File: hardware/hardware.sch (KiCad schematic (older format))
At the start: 6 parts

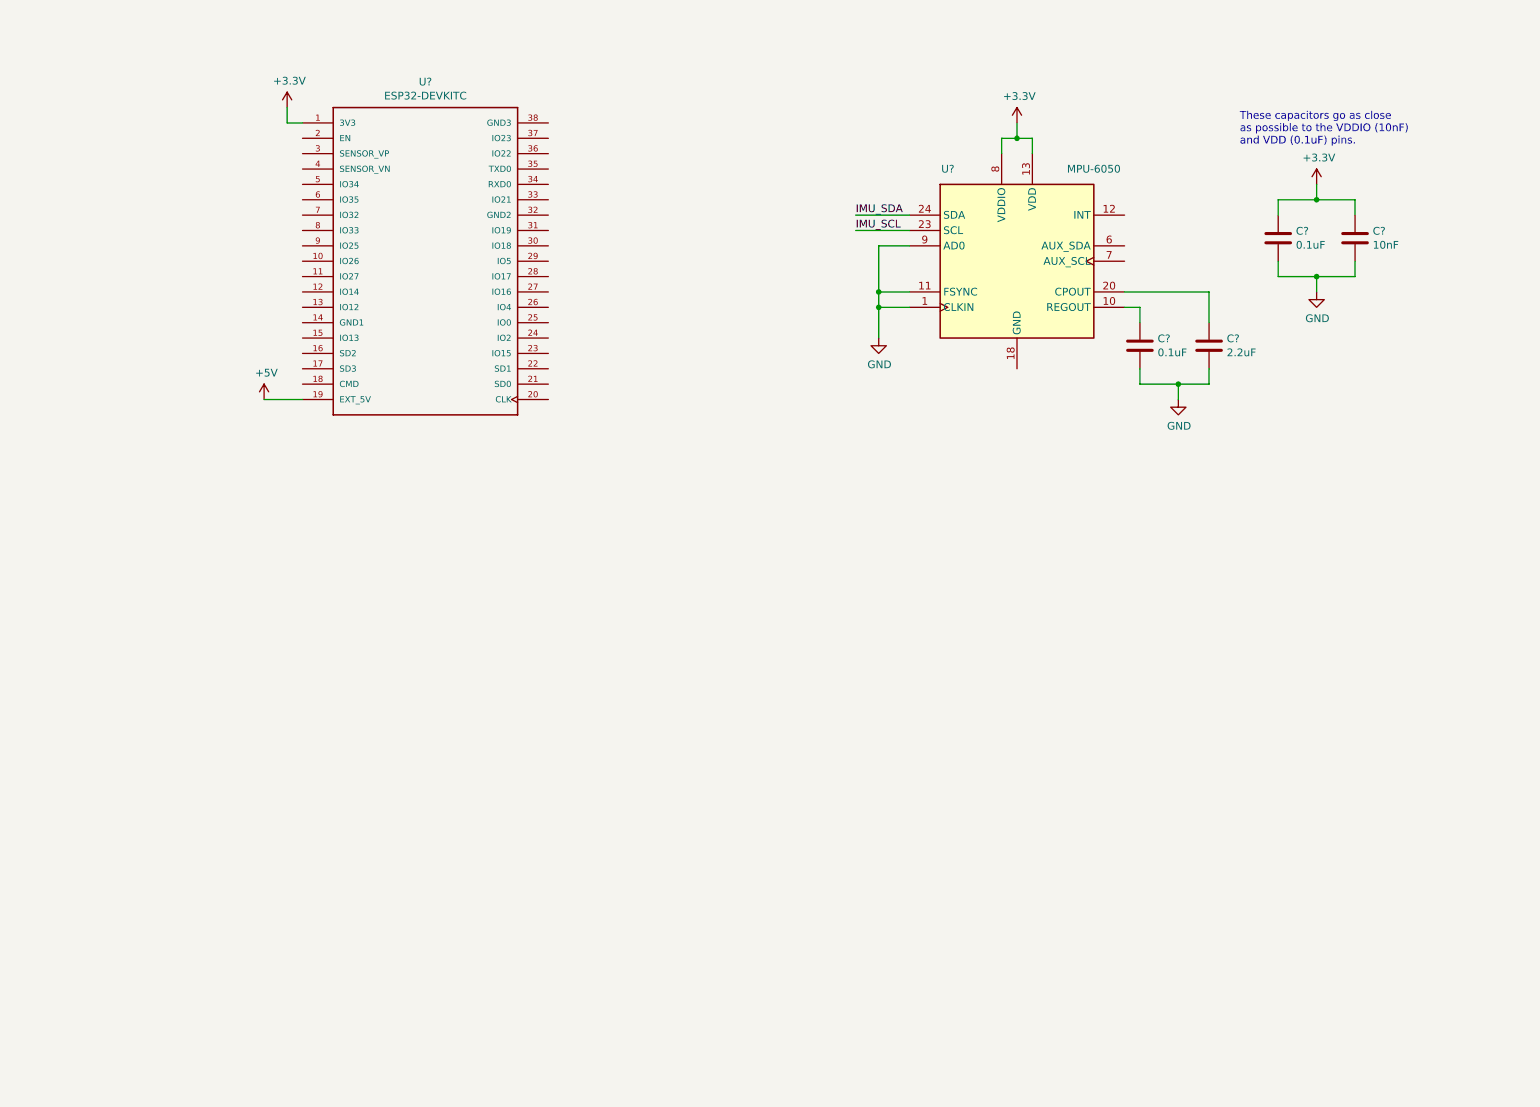
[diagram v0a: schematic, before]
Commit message: add cap sensor to schematic
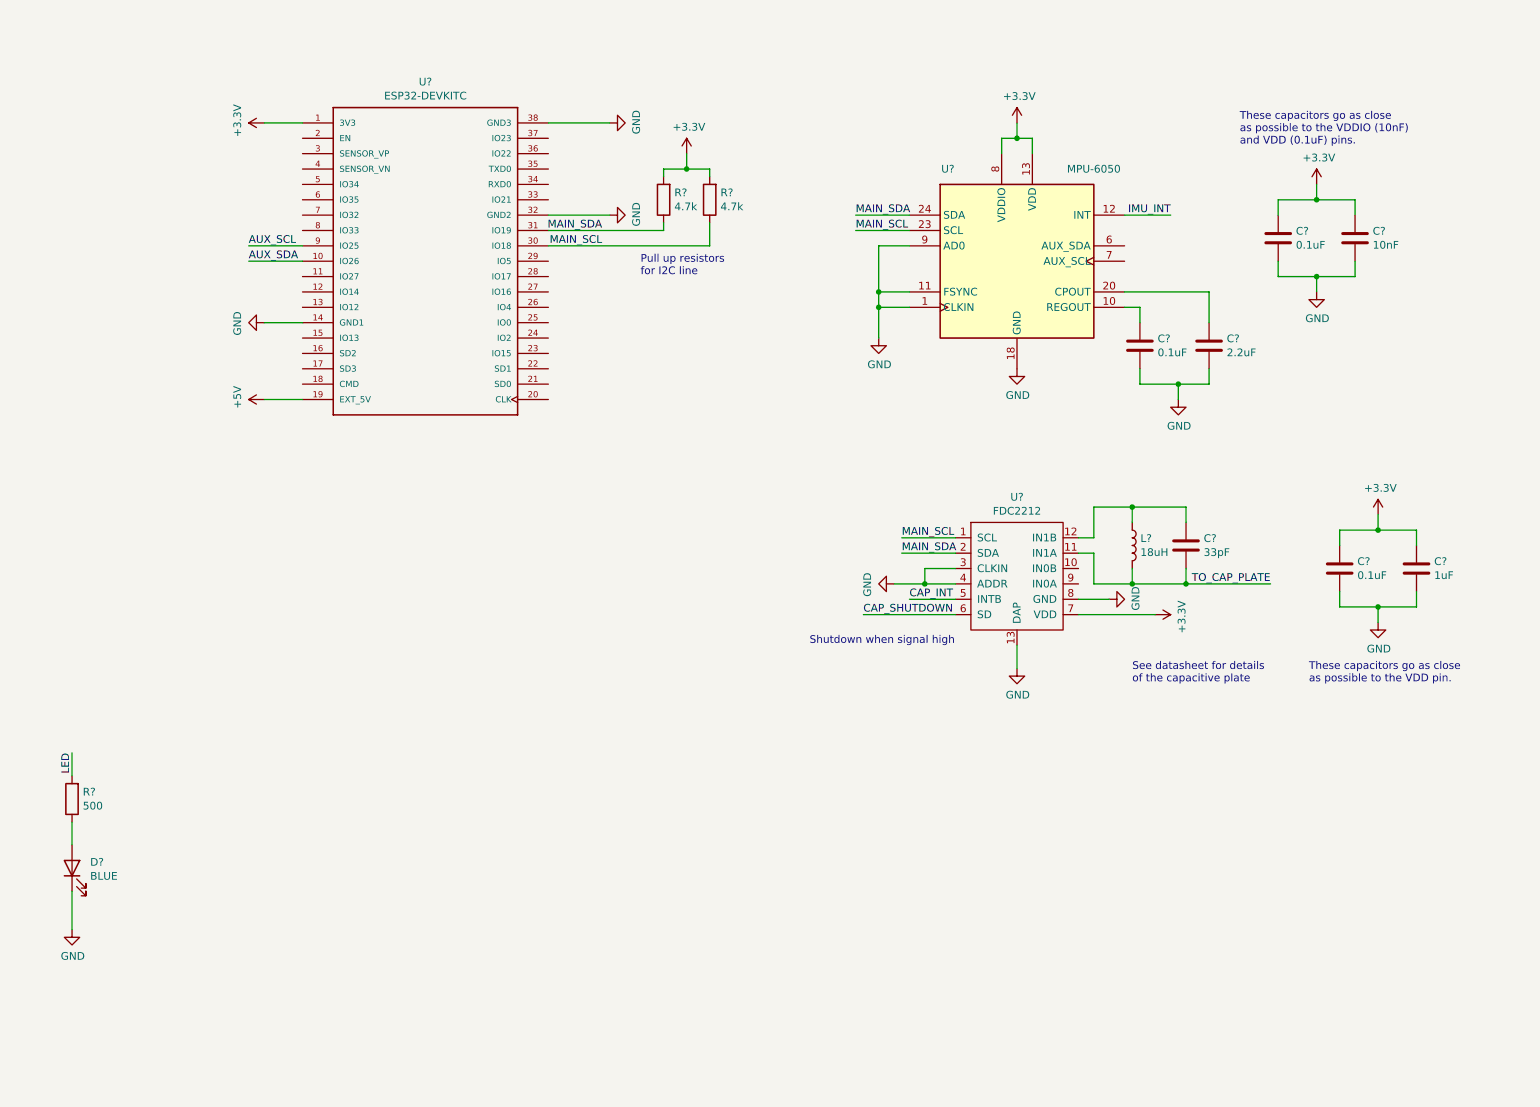
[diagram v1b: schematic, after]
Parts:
- added C?: 0.1uF, symbol Device:C
- added C?: 1uF, symbol Device:C
- added C?: 33pF, symbol Device:C
- added D?: BLUE, symbol Device:LED
- added L?: 18uH, symbol Device:L
- added R?: 500, symbol Device:R
- added R? (x2): 4.7k, symbol Device:R
- added U?: FDC2212, Package_SON:WSON-12-1EP_4x4mm_P0.5mm_EP2.6x3mm, symbol TI_FDC:FDC2212
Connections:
- net IMU_SCL is gone; now on net MAIN_SCL: U?.23 (SCL)
- net IMU_SDA is gone; now on net MAIN_SDA: U?.24 (SDA)
- net +3V3: now also C?.2, C?.2, R?.2, R?.2, U?.7 (VDD)
- net GND: now also U?.14 (GND1), U?.18 (GND), U?.32 (GND2), U?.38 (GND3), C?.1, C?.1, D?.1 (K), U?.13 (DAP), U?.3 (CLKIN), U?.4 (ADDR), U?.8 (GND)
- net AUX_SDA: now reaches U?.10 (IO26)
- net MAIN_SCL: now reaches U?.30 (IO18)
- net MAIN_SCL: now also R?.1, U?.1 (SCL)
- net MAIN_SDA: now reaches U?.31 (IO19)
- net MAIN_SDA: now also R?.1, U?.2 (SDA)
- net AUX_SCL: now reaches U?.9 (IO25)
- net IMU_INT: now reaches U?.12 (INT)
- new net: D?.2 (A), R?.1
- new net: C?.1, L?.1, U?.12 (IN1B)
- new net CAP_INT: U?.5 (INTB)
- new net CAP_SHUTDOWN: U?.6 (SD)
- new net LED: R?.2
- new net TO_CAP_PLATE: C?.2, L?.2, U?.11 (IN1A)
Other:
- note added: "Pull up resistors\nfor I2C line"
- note added: "See datasheet for details\nof the capacitive plate"
- note added: "Shutdown when signal high"
- note added: "These capacitors go as close\nas possible to the VDD pin."

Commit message: add acoustic and force sensor in schematic
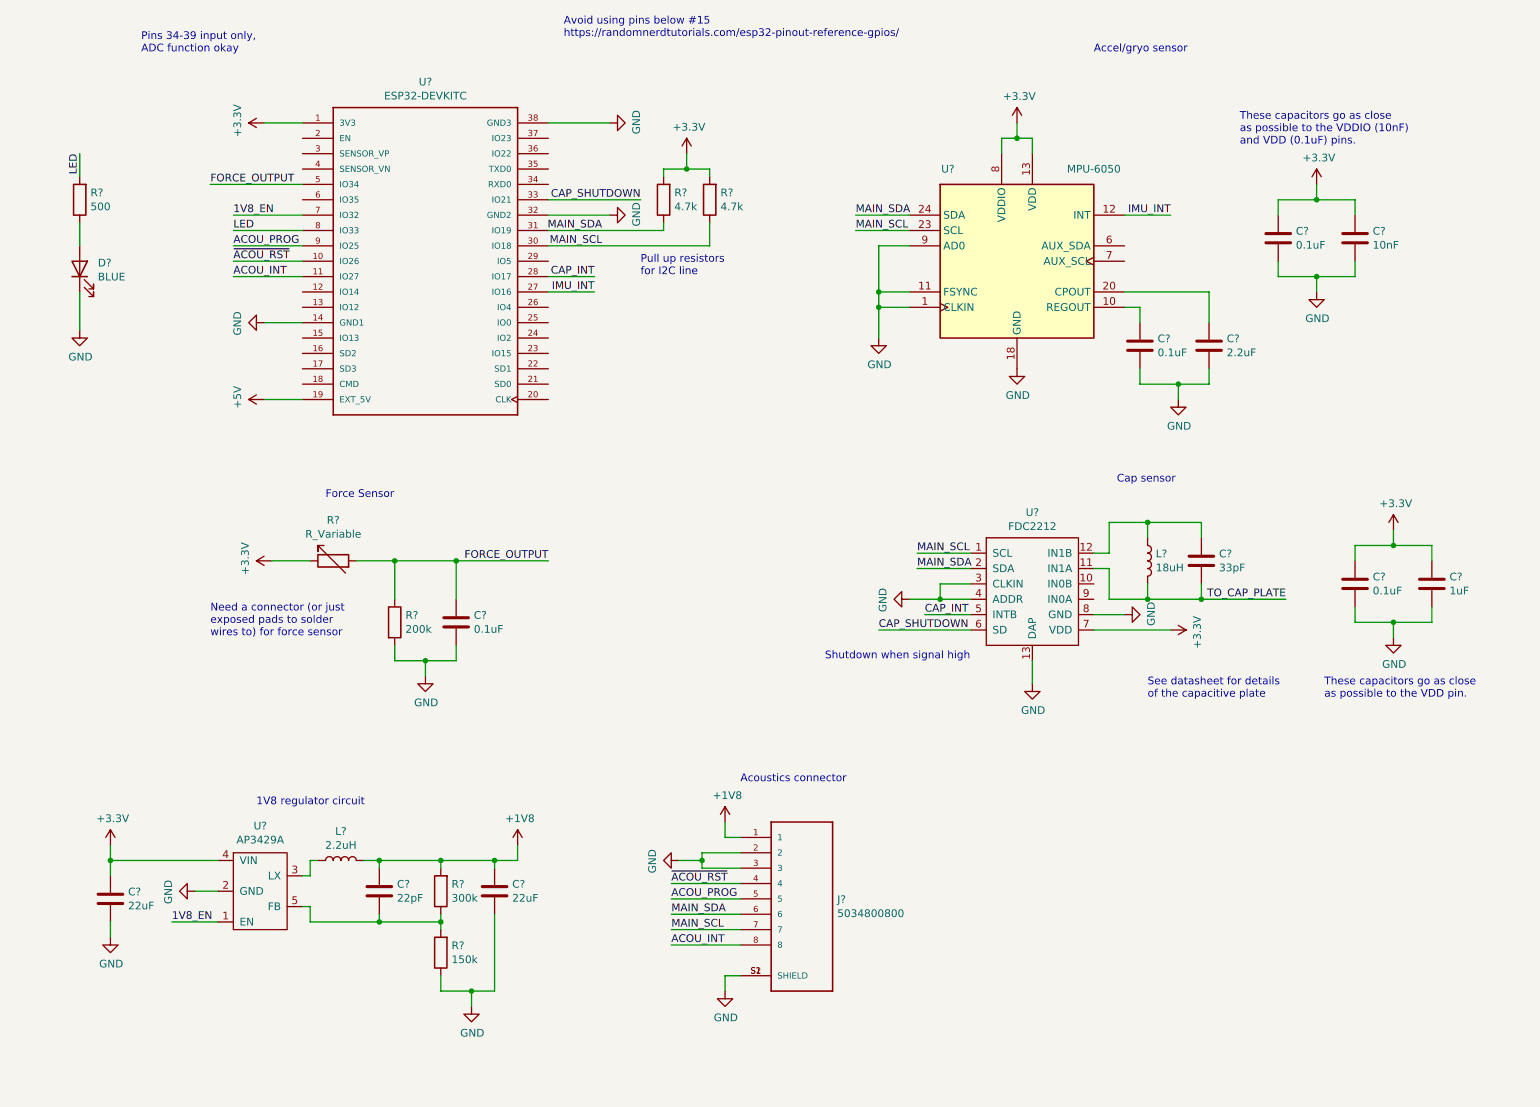
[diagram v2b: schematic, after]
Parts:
- added C? (x2): 22uF, symbol Device:C
- added C?: 22pF, symbol Device:C
- added C?: 0.1uF, symbol Device:C
- added J?: 5034800800, MOLEX_5034800800, symbol 5034800800:5034800800
- added L?: 2.2uH, symbol Device:L
- added R?: 300k, symbol Device:R
- added R?: 150k, symbol Device:R
- added R?: R_Variable, symbol Device:R_Variable
- added R?: 200k, symbol Device:R
- added U?: AP3429A, TSOT25:TSOT25, symbol AP3429A:AP3429A
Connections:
- net +3V3: now also C?.1, R?.1, U?.4 (VIN)
- net CAP_INT: now also U?.28 (IO17)
- net CAP_SHUTDOWN: now also U?.33 (IO21)
- net GND: now also C?.1, C?.2, C?.2, J?.2, J?.3, J?.S1 (SHIELD), J?.S2 (SHIELD), R?.1, R?.2, U?.2 (GND)
- net IMU_INT: now also U?.27 (IO16)
- net LED: now also U?.8 (IO33)
- net MAIN_SCL: now also J?.7
- net MAIN_SDA: now also J?.6
- net ACOU_INT: now reaches U?.11 (IO27)
- net ACOU_INT: now also J?.8
- net FORCE_OUTPUT: now reaches U?.5 (IO34)
- net FORCE_OUTPUT: now also C?.2, R?.1, R?.2
- net 1V8_EN: now reaches U?.7 (IO32)
- net 1V8_EN: now also U?.1 (EN)
- net AUX_SCL renamed ACOU_PROG
- net ACOU_PROG: now also J?.5
- net AUX_SDA renamed ~ACOU_RST
- net ~ACOU_RST: now also J?.4
- new net: L?.1, U?.3 (LX)
- new net: C?.2, R?.1, R?.2, U?.5 (FB)
- new net +1V8: C?.1, C?.1, J?.1, L?.2, R?.2
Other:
- note added: "1V8 regulator circuit"
- note added: "Accel/gryo sensor"
- note added: "Acoustics connector"
- note added: "Avoid using pins below #15\nhttps://randomnerdtutorials.com/esp32-pinout-reference-gpios/"
- note added: "Cap sensor"
- note added: "Force Sensor"
- note added: "Need a connector (or just\nexposed pads to solder\nwires to) for force sensor"
- note added: "Pins 34-39 input only,\nADC function okay"
- moved on the sheet: C?, D?, L?, R?, U?

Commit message: initial draft of schematic
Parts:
- J1: renamed from J?; footprint MOLEX_5034800800 -> external_footprints:MOLEX_5034800800
- U2: renamed from U?; footprint MODULE_ESP32-DEVKITC -> external_footprints:MODULE_ESP32-DEVKITC
- gave numbers to parts that had none: 24

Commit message: PCB Update 10/22
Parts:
- removed R2: R_Variable, symbol Device:R_Variable
- added H1, H2, H3, H4: MountingHole_Pad, MountingHole:MountingHole_3.2mm_M3_Pad, symbol Mechanical:MountingHole_Pad
- added H5, H6, H8, H9: Solder, MountingHole:MountingHole_2.2mm_M2_ISO14580_Pad, symbol Mechanical:MountingHole_Pad
- added H7: Solder (5V), MountingHole:MountingHole_2.2mm_M2_ISO14580_Pad, symbol Mechanical:MountingHole_Pad
- C1, C10, C11, C2, C3, C4, C5, C6, C7, C8, C9: footprint (none) -> Capacitor_SMD:C_0603_1608Metric_Pad1.05x0.95mm_HandSolder
- D1: footprint (none) -> LED_SMD:LED_0603_1608Metric_Pad1.05x0.95mm_HandSolder
- L1, L2: footprint (none) -> Inductor_SMD:L_0603_1608Metric_Pad1.05x0.95mm_HandSolder
- R1: value 500 -> 80; footprint (none) -> Resistor_SMD:R_1206_3216Metric
- R3, R4, R5, R6, R7: footprint (none) -> Resistor_SMD:R_0603_1608Metric_Pad1.05x0.95mm_HandSolder
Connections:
- net +3V3: now also H5.1
- net FORCE_OUTPUT: now also H6.1
- net GND: now also H1.1, H2.1, H3.1, H4.1, H8.1
- net TO_CAP_PLATE: now also H9.1
- net +5V: no longer names the net of U2.19 (EXT_5V)
- net +5V: now also H7.1

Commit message: IO Output
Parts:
- added IO12, IO14: Solder, MountingHole:MountingHole_2.2mm_M2_ISO14580_Pad, symbol Mechanical:MountingHole_Pad
- renumbered H5 to 3V3, H7 to 5V1, H9 to Cap1, H6 to Force1, H8 to GND1
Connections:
- net at U2.12 (IO14): now also IO14.1
- net at U2.13 (IO12): now also IO12.1
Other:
- moved on the sheet: D1, R1
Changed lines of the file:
@@
 L Device:LED D1
 U 1 1 5F8DECDA
-P 1050 2400
-F 0 "D1" V 1089 2282 50  0000 R CNN
-F 1 "BLUE" V 998 2282 50  0000 R CNN
-F 2 "LED_SMD:LED_0603_1608Metric_Pad1.05x0.95mm_HandSolder" H 1050 2400 50  0001 C CNN
-F 3 "~" H 1050 2400 50  0001 C CNN
-	1    1050 2400
+P 1050 4200
+F 0 "D1" V 1089 4082 50  0000 R CNN
+F 1 "BLUE" V 998 4082 50  0000 R CNN
+F 2 "LED_SMD:LED_0603_1608Metric_Pad1.05x0.95mm_HandSolder" H 1050 4200 50  0001 C CNN
+F 3 "~" H 1050 4200 50  0001 C CNN
+	1    1050 4200
 	0    -1   -1   0
 $EndComp
@@
 L power:GND #PWR01
 U 1 1 5F8E14EC
-P 1050 2800
-F 0 "#PWR01" H 1050 2550 50  0001 C CNN
-F 1 "GND" H 1055 2627 50  0000 C CNN
-F 2 "" H 1050 2800 50  0001 C CNN
-F 3 "" H 1050 2800 50  0001 C CNN
-	1    1050 2800
+P 1050 4600
+F 0 "#PWR01" H 1050 4350 50  0001 C CNN
+F 1 "GND" H 1055 4427 50  0000 C CNN
+F 2 "" H 1050 4600 50  0001 C CNN
+F 3 "" H 1050 4600 50  0001 C CNN
+	1    1050 4600
 	1    0    0    -1
 $EndComp
@@
 L Device:R R1
 U 1 1 5F8E1D46
-P 1050 1950
-F 0 "R1" H 980 1904 50  0000 R CNN
-F 1 "80" H 980 1995 50  0000 R CNN
-F 2 "Resistor_SMD:R_1206_3216Metric" V 980 1950 50  0001 C CNN
-F 3 "~" H 1050 1950 50  0001 C CNN
-	1    1050 1950
+P 1050 3750
+F 0 "R1" H 980 3704 50  0000 R CNN
+F 1 "80" H 980 3795 50  0000 R CNN
+F 2 "Resistor_SMD:R_1206_3216Metric" V 980 3750 50  0001 C CNN
+F 3 "~" H 1050 3750 50  0001 C CNN
+	1    1050 3750
 	-1   0    0    1
 $EndComp
 Wire Wire Line
-	1050 2800 1050 2550
-Wire Wire Line
-	1050 2250 1050 2100
-Text Label 1050 1650 3    50   ~ 0
+	1050 4600 1050 4350
+Wire Wire Line
+	1050 4050 1050 3900
+Text Label 1050 3450 3    50   ~ 0
 LED
 Wire Wire Line
-	1050 1650 1050 1800
+	1050 3450 1050 3600
 $Comp
 L power:GND #PWR013
@@
 $EndComp
 $Comp
-L Mechanical:MountingHole_Pad H5
+L Mechanical:MountingHole_Pad 3V3
 U 1 1 5F9F653D
 P 2100 4050
-F 0 "H5" H 2200 4099 50  0000 L CNN
+F 0 "3V3" H 2200 4099 50  0000 L CNN
 F 1 "Solder" H 2200 4008 50  0000 L CNN
 F 2 "MountingHole:MountingHole_2.2mm_M2_ISO14580_Pad" H 2100 4050 50  0001 C CNN
@@
 	2850 4300 2850 4150
 $Comp
-L Mechanical:MountingHole_Pad H6
+L Mechanical:MountingHole_Pad Force1
 U 1 1 5FA0FFF6
 P 2850 4050
-F 0 "H6" H 2950 4099 50  0000 L CNN
+F 0 "Force1" H 2950 4099 50  0000 L CNN
 F 1 "Solder" H 2950 4008 50  0000 L CNN
 F 2 "MountingHole:MountingHole_2.2mm_M2_ISO14580_Pad" H 2850 4050 50  0001 C CNN
@@
 $EndComp
 $Comp
-L Mechanical:MountingHole_Pad H8
+L Mechanical:MountingHole_Pad GND1
 U 1 1 5FA348EE
 P 5200 3900
-F 0 "H8" H 5300 3949 50  0000 L CNN
+F 0 "GND1" H 5300 3949 50  0000 L CNN
 F 1 "Solder" H 5300 3858 50  0000 L CNN
 F 2 "MountingHole:MountingHole_2.2mm_M2_ISO14580_Pad" H 5200 3900 50  0001 C CNN
@@
 	5200 4000 5200 4200
 $Comp
-L Mechanical:MountingHole_Pad H7
+L Mechanical:MountingHole_Pad 5V1
 U 1 1 5FA4435D
 P 1700 3050
-F 0 "H7" H 1800 3099 50  0000 L CNN
+F 0 "5V1" H 1800 3099 50  0000 L CNN
 F 1 "Solder (5V)" H 1800 3008 50  0000 L CNN
 F 2 "MountingHole:MountingHole_2.2mm_M2_ISO14580_Pad" H 1700 3050 50  0001 C CNN
@@
 	1700 3250 2500 3250
 $Comp
-L Mechanical:MountingHole_Pad H9
+L Mechanical:MountingHole_Pad Cap1
 U 1 1 5FA94347
 P 8900 3900
-F 0 "H9" H 9000 3949 50  0000 L CNN
+F 0 "Cap1" H 9000 3949 50  0000 L CNN
 F 1 "Solder" H 9000 3858 50  0000 L CNN
 F 2 "MountingHole:MountingHole_2.2mm_M2_ISO14580_Pad" H 8900 3900 50  0001 C CNN
@@
 Wire Wire Line
 	8900 4000 8900 4550
+$Comp
+L Mechanical:MountingHole_Pad IO12
+U 1 1 5F9AA3E5
+P 1300 1950
+F 0 "IO12" H 1400 1999 50  0000 L CNN
+F 1 "Solder" H 1400 1908 50  0000 L CNN
+F 2 "MountingHole:MountingHole_2.2mm_M2_ISO14580_Pad" H 1300 1950 50  0001 C CNN
+F 3 "~" H 1300 1950 50  0001 C CNN
+	1    1300 1950
+	1    0    0    -1
+$EndComp
+$Comp
+L Mechanical:MountingHole_Pad IO14
+U 1 1 5F9B1EF6
+P 1600 2250
+F 0 "IO14" H 1700 2299 50  0000 L CNN
+F 1 "Solder" H 1700 2208 50  0000 L CNN
+F 2 "MountingHole:MountingHole_2.2mm_M2_ISO14580_Pad" H 1600 2250 50  0001 C CNN
+F 3 "~" H 1600 2250 50  0001 C CNN
+	1    1600 2250
+	1    0    0    -1
+$EndComp
+Wire Wire Line
+	4100 2650 4550 2650
+Wire Wire Line
+	4550 2650 4550 2750
+Wire Wire Line
+	4550 2750 4750 2750
+Wire Wire Line
+	4100 2750 4450 2750
+Wire Wire Line
+	4450 2750 4450 3000
+Wire Wire Line
+	4450 3000 5150 3000
+Wire Wire Line
+	4100 2850 4350 2850
+Wire Wire Line
+	4350 2850 4350 3200
+Wire Wire Line
+	2500 2550 1600 2550
+Wire Wire Line
+	1600 2550 1600 2350
+Wire Wire Line
+	2500 2650 1300 2650
+Wire Wire Line
+	1300 2650 1300 2050
 $EndSCHEMATC
